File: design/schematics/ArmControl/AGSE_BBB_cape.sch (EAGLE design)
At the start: 56 parts, among them Q1 PFET-FQP27P06, Q2 PFET-FQP27P06, Q3 NFET-FQP30N06L, Q4 PFET-FQP27P06, Q5 NFET-FQP30N06L, Q6 PFET-FQP27P06, Q7 NFET-FQP30N06L, Q8 NFET-FQP30N06L, T1 2N2222, T2 2N2222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

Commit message: working on board layout
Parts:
- removed D3: GREEN, SparkFun-LED:LED-GREEN0603
- removed JP2: M023.5MM, SparkFun-Connectors:M023.5MM
- removed R3: 510, SparkFun-Passives:RESISTOR0402-RES
- removed X1: MKS1853-6-0-303, con-stocko:MKS1853-6-0-303
- Q4: value PFET-FQP27P06 -> NFET-FQP30N06L; device SparkFun-DiscreteSemi:MOSFET-PCHANNELFQP27P06 -> SparkFun-DiscreteSemi:MOSFET-NCHANNELFQP30N06L
- Q5: value NFET-FQP30N06L -> PFET-FQP27P06; device SparkFun-DiscreteSemi:MOSFET-NCHANNELFQP30N06L -> SparkFun-DiscreteSemi:MOSFET-PCHANNELFQP27P06
- R10, R11, R12, R13, R14, R15, R16, R17, R18, R19, R20, R21, R22, R23, R24, R4, R5, R6, R7, R8, R9: device resistor:R-EU_0207/12 -> resistor:R-EU_0204/2V
- T1, T2, T3, T4: value 2N2222 -> 2N3904; device transistor:2N2222 -> transistor:2N3904
- renumbered U$2 to SERVO
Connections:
- removed net N$2: D3.C, R3.2
- net 12V: now also Q5.S; no longer Q4.S
- net 5V: no longer D3.A, JP2.1
- net GND: now also Q4.S; no longer JP2.2, Q5.S, R3.1
- net N$1: now also Q6.D, Q8.D; no longer Q1.D, Q3.D
- net N$11: now also Q2.D, Q4.D; no longer Q6.D, Q7.D
- net N$12: now also Q1.D, Q3.D; no longer Q2.D, Q8.D
- net N$13: now also Q1.G, Q3.G; no longer Q2.G, Q8.G
- net N$14: now also Q2.G, Q4.G; no longer Q6.G, Q7.G
- net N$6: now also Q7.D; no longer Q4.D
- net N$7: now also Q7.G; no longer Q4.G
- net N$8: now also Q6.G, Q8.G; no longer Q1.G, Q3.G
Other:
- moved on the sheet: Q1, Q2, Q3, Q4, Q5, Q6, Q7, Q8

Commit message: changed to SMD.  working on placement & routing
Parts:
- R10, R11, R12, R13, R14, R15, R16, R17, R18, R19, R20, R21, R22, R23, R24, R4, R5, R6, R7, R8, R9: device resistor:R-EU_0204/2V -> resistor:R-EU_M0805
- T1, T2, T3, T4, T5, T6: value 2N3904 -> (none); device transistor:2N3904 -> transistor:BF820-NPN-SOT23-BEC

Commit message: working on routing
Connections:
- net N$1 renamed Z-
- net N$11 renamed R-
- net N$12 renamed R+
- net N$6 renamed Z+
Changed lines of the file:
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@@
 </segment>
 </net>
-<net name="N$1" class="0">
+<net name="Z-" class="0">
 <segment>
 <pinref part="Q6" gate="G$1" pin="D"/>
@@
 </segment>
 </net>
-<net name="N$11" class="0">
+<net name="R-" class="0">
 <segment>
 <pinref part="Q2" gate="G$1" pin="D"/>
@@
 </segment>
 </net>
-<net name="N$12" class="0">
+<net name="R+" class="0">
 <segment>
 <pinref part="Q3" gate="G$1" pin="D"/>
@@
 </segment>
 </net>
-<net name="N$6" class="0">
+<net name="Z+" class="0">
 <segment>
 <pinref part="Q7" gate="G$1" pin="D"/>

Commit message: working on routing the cape
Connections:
- net GND: now also U$1.GND@7, U$1.GND@8
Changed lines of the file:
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@@
 <grid distance="0.1" unitdist="inch" unit="inch" style="lines" multiple="1" display="no" altdistance="0.01" altunitdist="inch" altunit="inch"/>
 <layers>
-<layer number="1" name="Top" color="4" fill="1" visible="yes" active="no"/>
-<layer number="2" name="Route2" color="1" fill="3" visible="yes" active="no"/>
-<layer number="3" name="Route3" color="4" fill="3" visible="yes" active="no"/>
-<layer number="14" name="Route14" color="1" fill="6" visible="yes" active="no"/>
-<layer number="15" name="Route15" color="4" fill="6" visible="yes" active="no"/>
-<layer number="16" name="Bottom" color="1" fill="1" visible="yes" active="no"/>
-<layer number="17" name="Pads" color="2" fill="1" visible="yes" active="no"/>
-<layer number="18" name="Vias" color="2" fill="1" visible="yes" active="no"/>
-<layer number="19" name="Unrouted" color="6" fill="1" visible="yes" active="no"/>
-<layer number="20" name="Dimension" color="15" fill="1" visible="yes" active="no"/>
-<layer number="21" name="tPlace" color="7" fill="1" visible="yes" active="no"/>
-<layer number="22" name="bPlace" color="7" fill="1" visible="yes" active="no"/>
-<layer number="23" name="tOrigins" color="15" fill="1" visible="yes" active="no"/>
-<layer number="24" name="bOrigins" color="15" fill="1" visible="yes" active="no"/>
-<layer number="25" name="tNames" color="7" fill="1" visible="yes" active="no"/>
-<layer number="26" name="bNames" color="7" fill="1" visible="yes" active="no"/>
-<layer number="27" name="tValues" color="7" fill="1" visible="yes" active="no"/>
-<layer number="28" name="bValues" color="7" fill="1" visible="yes" active="no"/>
+<layer number="1" name="Top" color="4" fill="1" visible="no" active="no"/>
+<layer number="2" name="Route2" color="1" fill="3" visible="no" active="no"/>
+<layer number="3" name="Route3" color="4" fill="3" visible="no" active="no"/>
+<layer number="14" name="Route14" color="1" fill="6" visible="no" active="no"/>
+<layer number="15" name="Route15" color="4" fill="6" visible="no" active="no"/>
+<layer number="16" name="Bottom" color="1" fill="1" visible="no" active="no"/>
+<layer number="17" name="Pads" color="2" fill="1" visible="no" active="no"/>
+<layer number="18" name="Vias" color="2" fill="1" visible="no" active="no"/>
+<layer number="19" name="Unrouted" color="6" fill="1" visible="no" active="no"/>
+<layer number="20" name="Dimension" color="15" fill="1" visible="no" active="no"/>
+<layer number="21" name="tPlace" color="7" fill="1" visible="no" active="no"/>
+<layer number="22" name="bPlace" color="7" fill="1" visible="no" active="no"/>
+<layer number="23" name="tOrigins" color="15" fill="1" visible="no" active="no"/>
+<layer number="24" name="bOrigins" color="15" fill="1" visible="no" active="no"/>
+<layer number="25" name="tNames" color="7" fill="1" visible="no" active="no"/>
+<layer number="26" name="bNames" color="7" fill="1" visible="no" active="no"/>
+<layer number="27" name="tValues" color="7" fill="1" visible="no" active="no"/>
+<layer number="28" name="bValues" color="7" fill="1" visible="no" active="no"/>
 <layer number="29" name="tStop" color="7" fill="3" visible="no" active="no"/>
 <layer number="30" name="bStop" color="7" fill="6" visible="no" active="no"/>
@@
 <layer number="35" name="tGlue" color="7" fill="4" visible="no" active="no"/>
 <layer number="36" name="bGlue" color="7" fill="5" visible="no" active="no"/>
-<layer number="37" name="tTest" color="7" fill="1" visible="yes" active="no"/>
-<layer number="38" name="bTest" color="7" fill="1" visible="yes" active="no"/>
+<layer number="37" name="tTest" color="7" fill="1" visible="no" active="no"/>
+<layer number="38" name="bTest" color="7" fill="1" visible="no" active="no"/>
 <layer number="39" name="tKeepout" color="4" fill="11" visible="no" active="no"/>
 <layer number="40" name="bKeepout" color="1" fill="11" visible="no" active="no"/>
@@
 <layer number="44" name="Drills" color="7" fill="1" visible="no" active="no"/>
 <layer number="45" name="Holes" color="7" fill="1" visible="no" active="no"/>
-<layer number="46" name="Milling" color="3" fill="1" visible="yes" active="no"/>
-<layer number="47" name="Measures" color="7" fill="1" visible="yes" active="no"/>
-<layer number="48" name="Document" color="7" fill="1" visible="yes" active="no"/>
-<layer number="49" name="Reference" color="7" fill="1" visible="yes" active="no"/>
-<layer number="50" name="dxf" color="7" fill="1" visible="yes" active="no"/>
-<layer number="51" name="tDocu" color="7" fill="1" visible="yes" active="no"/>
-<layer number="52" name="bDocu" color="7" fill="1" visible="yes" active="no"/>
-<layer number="53" name="tGND_GNDA" color="7" fill="9" visible="yes" active="no"/>
-<layer number="54" name="bGND_GNDA" color="1" fill="9" visible="yes" active="no"/>
-<layer number="56" name="wert" color="7" fill="1" visible="yes" active="no"/>
-<layer number="57" name="tCAD" color="7" fill="1" visible="yes" active="no"/>
+<layer number="46" name="Milling" color="3" fill="1" visible="no" active="no"/>
+<layer number="47" name="Measures" color="7" fill="1" visible="no" active="no"/>
+<layer number="48" name="Document" color="7" fill="1" visible="no" active="no"/>
+<layer number="49" name="Reference" color="7" fill="1" visible="no" active="no"/>
+<layer number="50" name="dxf" color="7" fill="1" visible="no" active="no"/>
+<layer number="51" name="tDocu" color="7" fill="1" visible="no" active="no"/>
+<layer number="52" name="bDocu" color="7" fill="1" visible="no" active="no"/>
+<layer number="53" name="tGND_GNDA" color="7" fill="9" visible="no" active="no"/>
+<layer number="54" name="bGND_GNDA" color="1" fill="9" visible="no" active="no"/>
+<layer number="56" name="wert" color="7" fill="1" visible="no" active="no"/>
+<layer number="57" name="tCAD" color="7" fill="1" visible="no" active="no"/>
 <layer number="90" name="Modules" color="5" fill="1" visible="yes" active="yes"/>
 <layer number="91" name="Nets" color="2" fill="1" visible="yes" active="yes"/>
@@
 <wire x1="266.7" y1="73.66" x2="266.7" y2="66.04" width="0.1524" layer="91"/>
 <junction x="266.7" y="73.66"/>
+<pinref part="U$1" gate="G$1" pin="GND@7"/>
+<wire x1="266.7" y1="129.54" x2="266.7" y2="195.58" width="0.1524" layer="91"/>
+<wire x1="266.7" y1="195.58" x2="274.32" y2="195.58" width="0.1524" layer="91"/>
+<junction x="266.7" y="129.54"/>
 </segment>
 <segment>
@@
 <wire x1="340.36" y1="66.04" x2="340.36" y2="73.66" width="0.1524" layer="91"/>
 <junction x="340.36" y="73.66"/>
+<pinref part="U$1" gate="G$1" pin="GND@8"/>
+<wire x1="340.36" y1="129.54" x2="340.36" y2="195.58" width="0.1524" layer="91"/>
+<wire x1="340.36" y1="195.58" x2="330.2" y2="195.58" width="0.1524" layer="91"/>
+<junction x="340.36" y="129.54"/>
 </segment>
 <segment>
@@
 <segment>
 <pinref part="U$1" gate="G$1" pin="GPIO2_24"/>
-<wire x1="330.2" y1="162.56" x2="340.36" y2="162.56" width="0.1524" layer="91"/>
-<label x="340.36" y="162.56" size="1.778" layer="95"/>
+<wire x1="330.2" y1="162.56" x2="342.9" y2="162.56" width="0.1524" layer="91"/>
+<label x="342.9" y="162.56" size="1.778" layer="95"/>
 </segment>
 </net>
@@
 <segment>
 <pinref part="U$1" gate="G$1" pin="GPIO2_25"/>
-<wire x1="330.2" y1="160.02" x2="340.36" y2="160.02" width="0.1524" layer="91"/>
-<label x="340.36" y="160.02" size="1.778" layer="95"/>
+<wire x1="330.2" y1="160.02" x2="342.9" y2="160.02" width="0.1524" layer="91"/>
+<label x="342.9" y="160.02" size="1.778" layer="95"/>
 </segment>
 </net>
@@
 <segment>
 <pinref part="U$1" gate="G$1" pin="GPIO1_12"/>
-<wire x1="330.2" y1="182.88" x2="340.36" y2="182.88" width="0.1524" layer="91"/>
-<label x="340.36" y="182.88" size="1.778" layer="95"/>
-</segment>
-</net>
+<wire x1="330.2" y1="182.88" x2="342.9" y2="182.88" width="0.1524" layer="91"/>
+<label x="342.9" y="182.88" size="1.778" layer="95"/>
+</segment>
+</net>

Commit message: routed the board, cleaned up the names and made ready for fab.
also added sparkfun's DRU for checking fab-ability
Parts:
- removed FID1, FID2, FID3: FIDUCIAL1X2, SparkFun-Aesthetics:FIDUCIAL1X2
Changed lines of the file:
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@@
 <part name="GND7" library="SparkFun-Aesthetics" deviceset="GND" device=""/>
 <part name="SUPPLY3" library="SparkFun-Aesthetics" deviceset="5V" device=""/>
-<part name="FID1" library="SparkFun-Aesthetics" deviceset="FIDUCIAL" device="1X2"/>
-<part name="FID2" library="SparkFun-Aesthetics" deviceset="FIDUCIAL" device="1X2"/>
-<part name="FID3" library="SparkFun-Aesthetics" deviceset="FIDUCIAL" device="1X2"/>
 <part name="P+2" library="supply1" deviceset="+5V" device="" value="+12V"/>
 <part name="GND9" library="supply1" deviceset="GND" device=""/>
@@
 <instance part="GND7" gate="1" x="0" y="-2.54"/>
 <instance part="SUPPLY3" gate="G$1" x="345.44" y="132.08"/>
-<instance part="FID1" gate="G$1" x="81.28" y="0"/>
-<instance part="FID2" gate="G$1" x="86.36" y="0"/>
-<instance part="FID3" gate="G$1" x="91.44" y="0"/>
 <instance part="P+2" gate="1" x="180.34" y="12.7" smashed="yes">
 <attribute name="VALUE" x="182.245" y="15.24" size="1.778" layer="96" rot="R180"/>

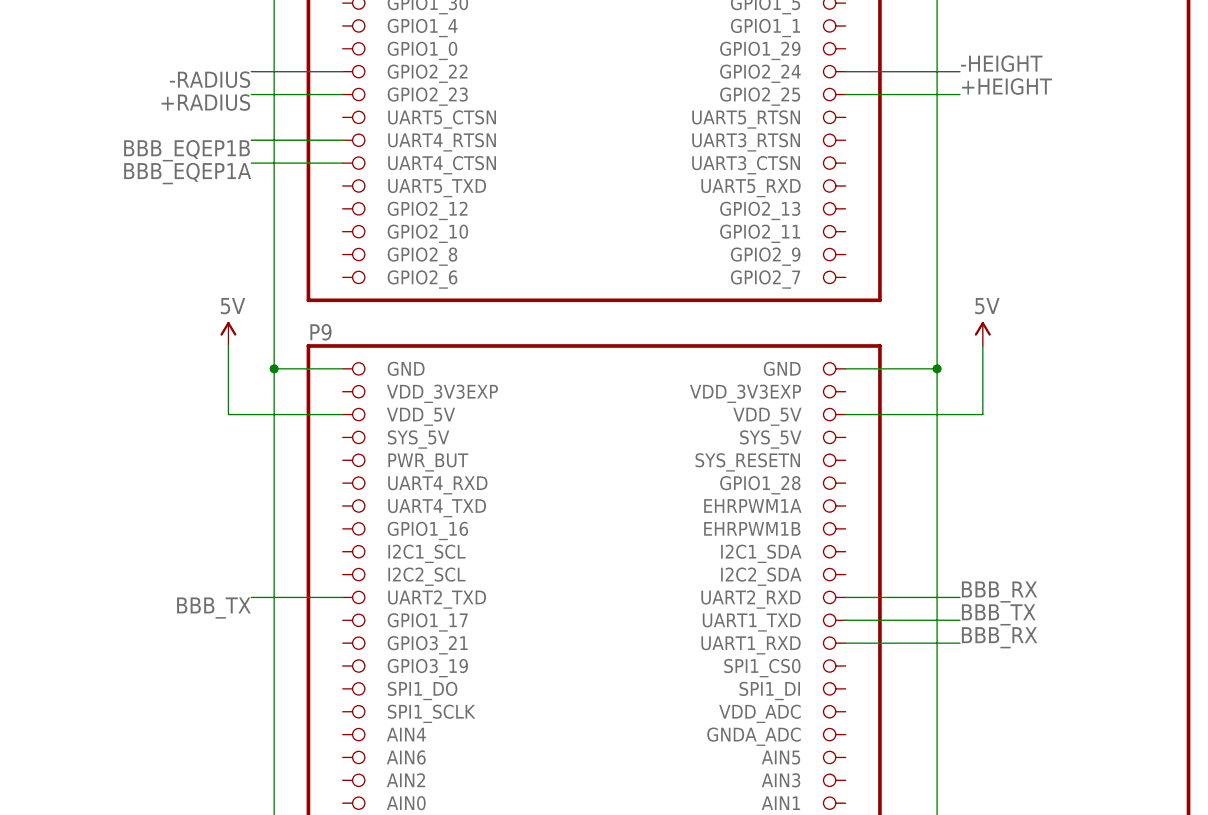
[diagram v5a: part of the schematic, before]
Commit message: updated schematic to move tx/rx connection from UART1 to UART5
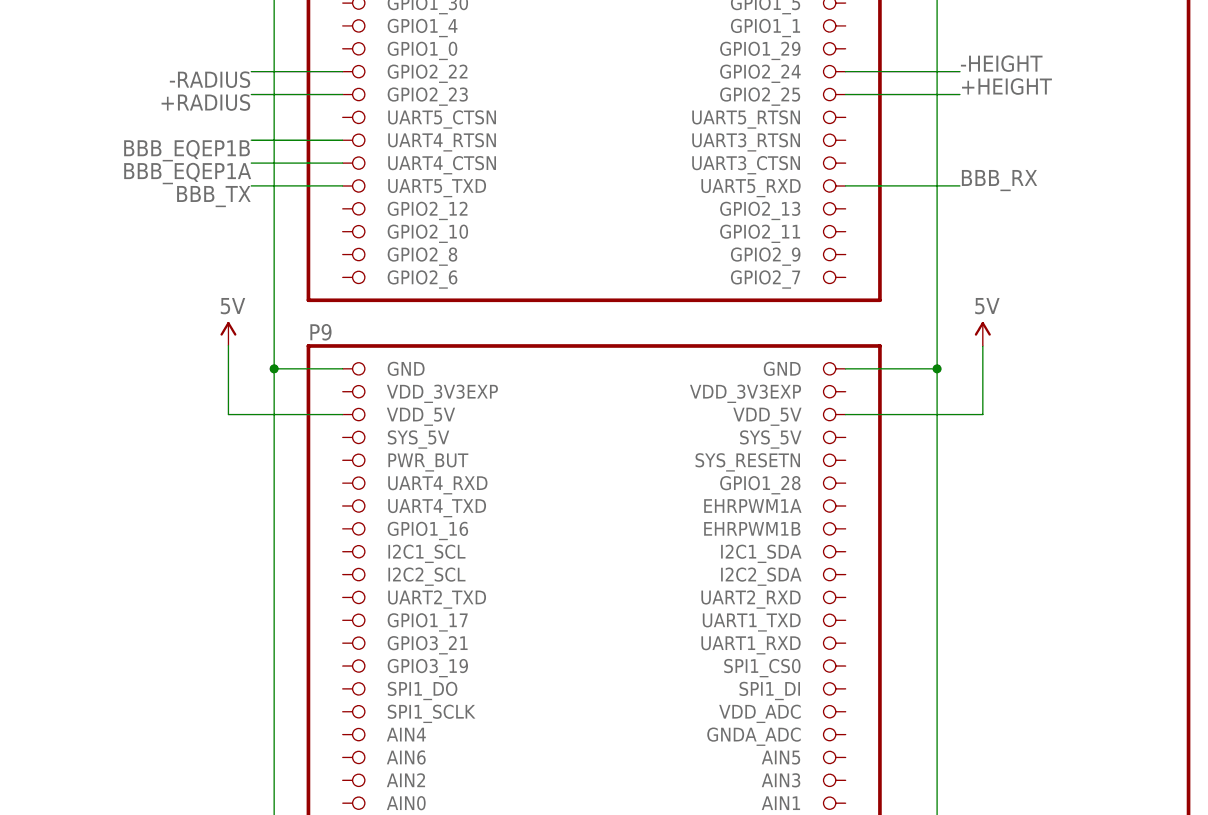
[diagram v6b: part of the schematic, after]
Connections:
- net BBB_RX: now also U$1.UART5_RXD; no longer U$1.UART1_RXD, U$1.UART2_RXD
- net BBB_TX: now also U$1.UART5_TXD; no longer U$1.UART1_TXD, U$1.UART2_TXD
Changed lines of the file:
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@@
 </segment>
 <segment>
-<pinref part="U$1" gate="G$1" pin="UART2_RXD"/>
-<wire x1="330.2" y1="104.14" x2="342.9" y2="104.14" width="0.1524" layer="91"/>
-<label x="342.9" y="104.14" size="1.778" layer="95"/>
-</segment>
-<segment>
-<pinref part="U$1" gate="G$1" pin="UART1_RXD"/>
-<wire x1="330.2" y1="99.06" x2="342.9" y2="99.06" width="0.1524" layer="91"/>
-<label x="342.9" y="99.06" size="1.778" layer="95"/>
+<pinref part="U$1" gate="G$1" pin="UART5_RXD"/>
+<wire x1="330.2" y1="149.86" x2="342.9" y2="149.86" width="0.1524" layer="91"/>
+<label x="342.9" y="149.86" size="1.778" layer="95"/>
 </segment>
 </net>
@@
 </segment>
 <segment>
-<pinref part="U$1" gate="G$1" pin="UART2_TXD"/>
-<wire x1="274.32" y1="104.14" x2="264.16" y2="104.14" width="0.1524" layer="91"/>
-<label x="264.16" y="104.14" size="1.778" layer="95" rot="R180"/>
-</segment>
-<segment>
-<pinref part="U$1" gate="G$1" pin="UART1_TXD"/>
-<wire x1="330.2" y1="101.6" x2="342.9" y2="101.6" width="0.1524" layer="91"/>
-<label x="342.9" y="101.6" size="1.778" layer="95"/>
+<pinref part="U$1" gate="G$1" pin="UART5_TXD"/>
+<wire x1="274.32" y1="149.86" x2="264.16" y2="149.86" width="0.1524" layer="91"/>
+<label x="264.16" y="149.86" size="1.778" layer="95" rot="R180"/>
 </segment>
 </net>
